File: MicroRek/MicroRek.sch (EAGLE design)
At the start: 41 parts, among them IC3 LSM9DS1TR

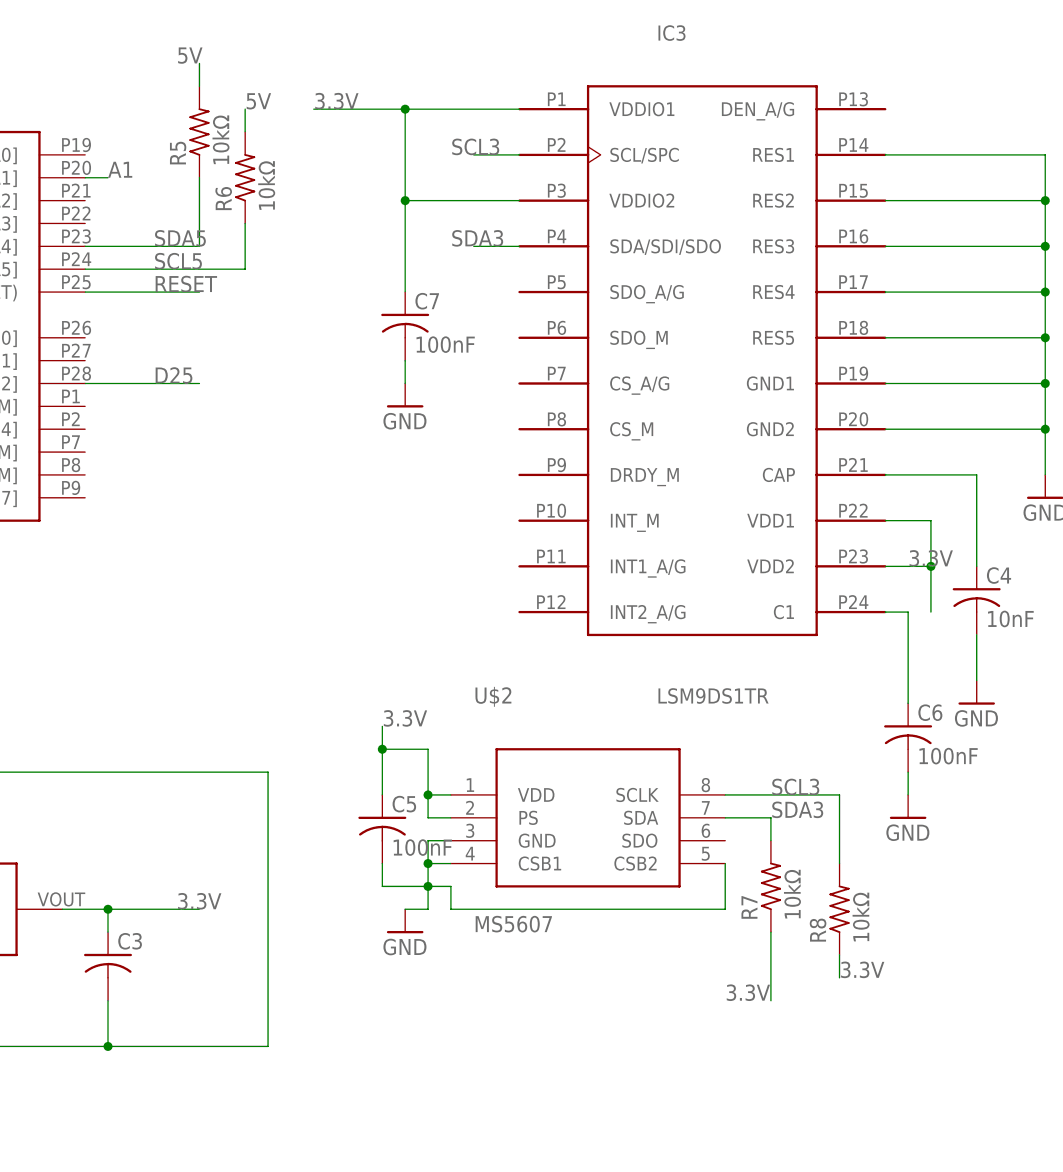
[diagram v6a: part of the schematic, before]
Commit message: fixed pullup resistors
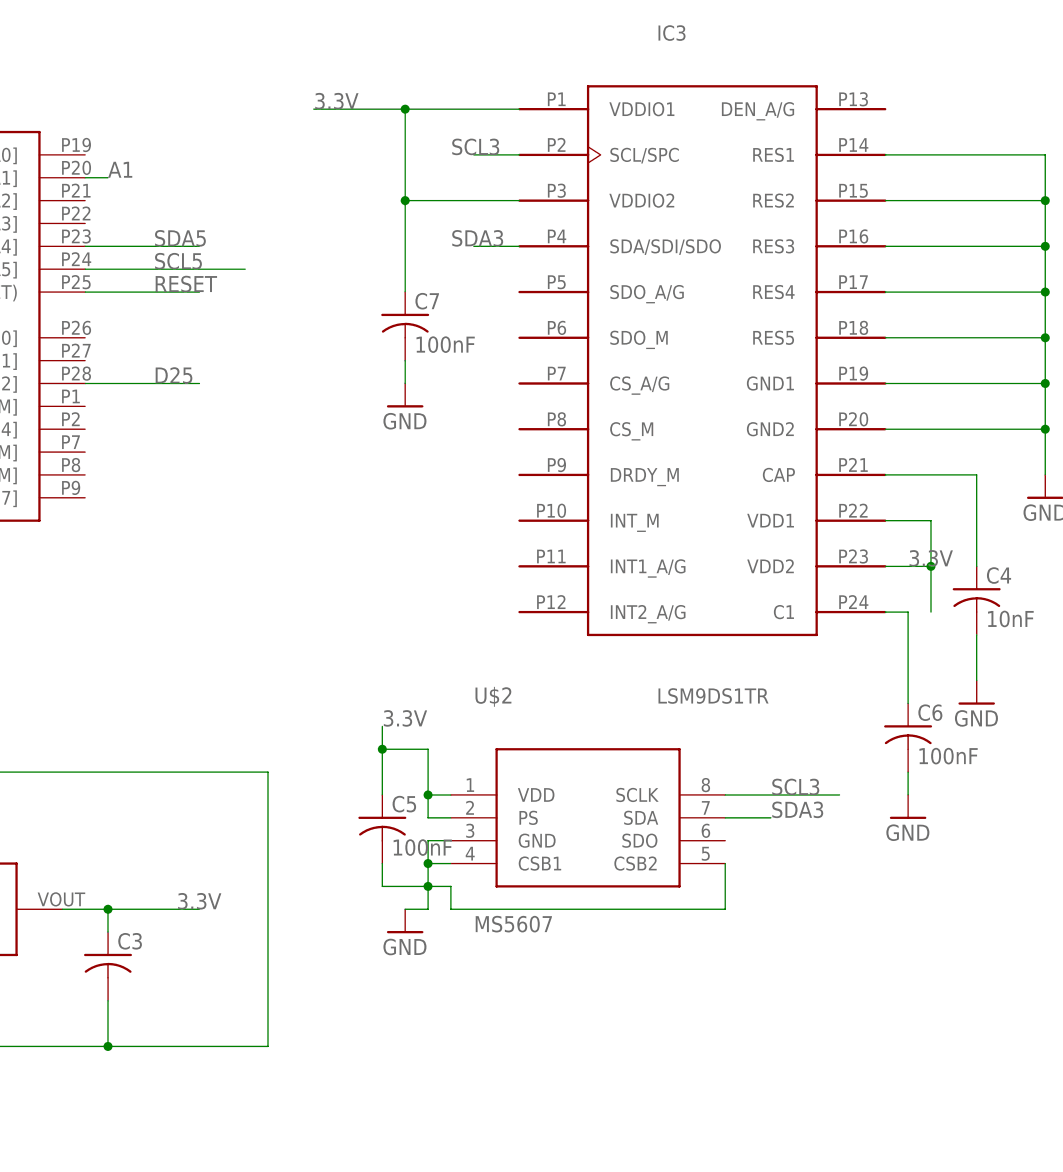
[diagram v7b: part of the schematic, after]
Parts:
- removed R5, R6, R7, R8: 10kΩ, resistor:R-US_R0603
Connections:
- net 3.3V: no longer R7.1, R8.1
- net 5V: no longer R5.2, R6.2
- net SCL3: no longer R8.2
- net SCL5: no longer R6.1
- net SDA3: no longer R7.2
- net SDA5: no longer R5.1
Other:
- note removed: "0805 LED"
- note removed: "100ohm for R3 100kohm for R2 4.7kohm R1 For LEDS"
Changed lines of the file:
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@@
 <part name="L1" library="CPSS" deviceset="L-US" device="" value="4.7 uH"/>
 <part name="R4" library="resistor" library_urn="urn:adsk.eagle:library:348" deviceset="R-US_" device="R0603" package3d_urn="urn:adsk.eagle:package:26057/1" value="100KΩ"/>
-<part name="R5" library="resistor" library_urn="urn:adsk.eagle:library:348" deviceset="R-US_" device="R0603" package3d_urn="urn:adsk.eagle:package:26057/1" value="10kΩ"/>
-<part name="R6" library="resistor" library_urn="urn:adsk.eagle:library:348" deviceset="R-US_" device="R0603" package3d_urn="urn:adsk.eagle:package:26057/1" value="10kΩ"/>
-<part name="R7" library="resistor" library_urn="urn:adsk.eagle:library:348" deviceset="R-US_" device="R0603" package3d_urn="urn:adsk.eagle:package:26057/1" value="10kΩ"/>
-<part name="R8" library="resistor" library_urn="urn:adsk.eagle:library:348" deviceset="R-US_" device="R0603" package3d_urn="urn:adsk.eagle:package:26057/1" value="10kΩ"/>
 <part name="U$8" library="CPSS_CONNECTOR" deviceset="MINI_ICSP" device=""/>
 <part name="GND10" library="supply1" library_urn="urn:adsk.eagle:library:371" deviceset="GND" device=""/>
@@
 <plain>
 <frame x1="0" y1="0" x2="279.4" y2="215.9" columns="8" rows="5" layer="97"/>
-<text x="193.04" y="83.82" size="1.778" layer="101">100ohm for R3
-100kohm for R2
-4.7kohm R1
-For LEDS</text>
-<text x="193.04" y="78.74" size="1.778" layer="101">0805 LED</text>
 </plain>
 <instances>
@@
 <instance part="L1" gate="G$1" x="96.52" y="109.22" rot="R90"/>
 <instance part="R4" gate="G$1" x="162.56" y="68.58"/>
-<instance part="R5" gate="G$1" x="167.64" y="195.58" rot="R90"/>
-<instance part="R6" gate="G$1" x="172.72" y="190.5" rot="R90"/>
-<instance part="R7" gate="G$1" x="231.14" y="111.76" rot="R90"/>
-<instance part="R8" gate="G$1" x="238.76" y="109.22" rot="R90"/>
 <instance part="U$8" gate="G$1" x="121.92" y="137.16"/>
 <instance part="GND10" gate="1" x="139.7" y="129.54"/>
@@
 </segment>
 <segment>
-<pinref part="R5" gate="G$1" pin="2"/>
-<wire x1="167.64" y1="200.66" x2="167.64" y2="203.2" width="0.1524" layer="91"/>
-<label x="165.1" y="203.2" size="1.778" layer="95"/>
-</segment>
-<segment>
-<pinref part="R6" gate="G$1" pin="2"/>
-<wire x1="172.72" y1="195.58" x2="172.72" y2="198.12" width="0.1524" layer="91"/>
-<label x="172.72" y="198.12" size="1.778" layer="95"/>
-</segment>
-<segment>
 <pinref part="R14" gate="G$1" pin="2"/>
 <wire x1="78.74" y1="68.58" x2="81.28" y2="68.58" width="0.1524" layer="91"/>
@@
 <wire x1="154.94" y1="182.88" x2="167.64" y2="182.88" width="0.1524" layer="91"/>
 <label x="162.56" y="182.88" size="1.778" layer="95"/>
-<wire x1="167.64" y1="182.88" x2="167.64" y2="190.5" width="0.1524" layer="91"/>
-<pinref part="R5" gate="G$1" pin="1"/>
 </segment>
 </net>
@@
 <wire x1="154.94" y1="180.34" x2="172.72" y2="180.34" width="0.1524" layer="91"/>
 <label x="162.56" y="180.34" size="1.778" layer="95"/>
-<wire x1="172.72" y1="180.34" x2="172.72" y2="185.42" width="0.1524" layer="91"/>
-<pinref part="R6" gate="G$1" pin="1"/>
 </segment>
 </net>
@@
 <wire x1="226.06" y1="119.38" x2="231.14" y2="119.38" width="0.1524" layer="91"/>
 <label x="231.14" y="119.38" size="1.778" layer="95"/>
-<wire x1="231.14" y1="119.38" x2="231.14" y2="116.84" width="0.1524" layer="91"/>
-<pinref part="R7" gate="G$1" pin="2"/>
 </segment>
 <segment>
@@
 <label x="231.14" y="121.92" size="1.778" layer="95"/>
 <wire x1="226.06" y1="121.92" x2="238.76" y2="121.92" width="0.1524" layer="91"/>
-<wire x1="238.76" y1="121.92" x2="238.76" y2="114.3" width="0.1524" layer="91"/>
-<pinref part="R8" gate="G$1" pin="2"/>
 </segment>
 <segment>
@@
 <label x="137.16" y="58.42" size="1.778" layer="95"/>
 </segment>
-<segment>
-<pinref part="R7" gate="G$1" pin="1"/>
-<wire x1="231.14" y1="106.68" x2="231.14" y2="99.06" width="0.1524" layer="91"/>
-<label x="226.06" y="99.06" size="1.778" layer="95"/>
-</segment>
-<segment>
-<pinref part="R8" gate="G$1" pin="1"/>
-<wire x1="238.76" y1="104.14" x2="238.76" y2="101.6" width="0.1524" layer="91"/>
-<label x="238.76" y="101.6" size="1.778" layer="95"/>
-</segment>
 </net>
 <net name="CPB6" class="0">
@@
 </drawing>
 <compatibility>
-<note version="6.3" minversion="6.2.2" severity="warning">
-Since Version 6.2.2 text objects can contain more than one line,
-which will not be processed correctly with this version.
-</note>
 <note version="8.2" severity="warning">
 Since Version 8.2, EAGLE supports online libraries. The ids

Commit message: Approved Final Schematic
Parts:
- removed R10, R11, R12, R17, R18, R19: 4.7kΩ, resistor:R-US_R0603
- R4: value 100KΩ -> 100Ω
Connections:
- net 3.3V: no longer R17.1, R18.1, R19.1
- net 5V: no longer R10.2, R11.2, R12.2
- net MISO3: no longer R19.2
- net MISO5: no longer R12.1
- net MOSI3: no longer R18.2
- net MOSI5: no longer R11.1
- net SCK3: no longer R17.2
- net SCK5: no longer R10.1
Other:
- moved on the sheet: R21
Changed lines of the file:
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@@
 <?xml version="1.0" encoding="utf-8"?>
 <!DOCTYPE eagle SYSTEM "eagle.dtd">
-<eagle version="9.0.0">
+<eagle version="8.7.1">
 <drawing>
 <settings>
-<setting alwaysvectorfont="no"/>
+<setting alwaysvectorfont="yes"/>
 <setting verticaltext="up"/>
 </settings>
@@
 <part name="LED2" library="led" library_urn="urn:adsk.eagle:library:259" deviceset="LED" device="CHIPLED_0805" package3d_urn="urn:adsk.eagle:package:15821/2"/>
 <part name="L1" library="CPSS" deviceset="L-US" device="" value="4.7 uH"/>
-<part name="R4" library="resistor" library_urn="urn:adsk.eagle:library:348" deviceset="R-US_" device="R0603" package3d_urn="urn:adsk.eagle:package:26057/1" value="100KΩ"/>
+<part name="R4" library="resistor" library_urn="urn:adsk.eagle:library:348" deviceset="R-US_" device="R0603" package3d_urn="urn:adsk.eagle:package:26057/1" value="100Ω"/>
 <part name="U$8" library="CPSS_CONNECTOR" deviceset="MINI_ICSP" device=""/>
 <part name="GND10" library="supply1" library_urn="urn:adsk.eagle:library:371" deviceset="GND" device=""/>
 <part name="R9" library="resistor" library_urn="urn:adsk.eagle:library:348" deviceset="R-US_" device="R0603" package3d_urn="urn:adsk.eagle:package:26057/1" value="4.7kΩ"/>
-<part name="R10" library="resistor" library_urn="urn:adsk.eagle:library:348" deviceset="R-US_" device="R0603" package3d_urn="urn:adsk.eagle:package:26057/1" value="4.7kΩ"/>
-<part name="R11" library="resistor" library_urn="urn:adsk.eagle:library:348" deviceset="R-US_" device="R0603" package3d_urn="urn:adsk.eagle:package:26057/1" value="4.7kΩ"/>
-<part name="R12" library="resistor" library_urn="urn:adsk.eagle:library:348" deviceset="R-US_" device="R0603" package3d_urn="urn:adsk.eagle:package:26057/1" value="4.7kΩ"/>
 <part name="R13" library="resistor" library_urn="urn:adsk.eagle:library:348" deviceset="R-US_" device="R0603" package3d_urn="urn:adsk.eagle:package:26057/1" value="4.7kΩ"/>
 <part name="R14" library="resistor" library_urn="urn:adsk.eagle:library:348" deviceset="R-US_" device="R0603" package3d_urn="urn:adsk.eagle:package:26057/1" value="4.7kΩ"/>
 <part name="R15" library="resistor" library_urn="urn:adsk.eagle:library:348" deviceset="R-US_" device="R0603" package3d_urn="urn:adsk.eagle:package:26057/1" value="4.7kΩ"/>
 <part name="R16" library="resistor" library_urn="urn:adsk.eagle:library:348" deviceset="R-US_" device="R0603" package3d_urn="urn:adsk.eagle:package:26057/1" value="4.7kΩ"/>
-<part name="R17" library="resistor" library_urn="urn:adsk.eagle:library:348" deviceset="R-US_" device="R0603" package3d_urn="urn:adsk.eagle:package:26057/1" value="4.7kΩ"/>
-<part name="R18" library="resistor" library_urn="urn:adsk.eagle:library:348" deviceset="R-US_" device="R0603" package3d_urn="urn:adsk.eagle:package:26057/1" value="4.7kΩ"/>
-<part name="R19" library="resistor" library_urn="urn:adsk.eagle:library:348" deviceset="R-US_" device="R0603" package3d_urn="urn:adsk.eagle:package:26057/1" value="4.7kΩ"/>
 <part name="R20" library="resistor" library_urn="urn:adsk.eagle:library:348" deviceset="R-US_" device="R0603" package3d_urn="urn:adsk.eagle:package:26057/1" value="4.7kΩ"/>
 <part name="GND2" library="supply1" library_urn="urn:adsk.eagle:library:371" deviceset="GND" device=""/>
@@
 <instance part="GND10" gate="1" x="139.7" y="129.54"/>
 <instance part="R9" gate="G$1" x="73.66" y="43.18"/>
-<instance part="R10" gate="G$1" x="73.66" y="48.26"/>
-<instance part="R11" gate="G$1" x="73.66" y="53.34"/>
-<instance part="R12" gate="G$1" x="73.66" y="58.42"/>
 <instance part="R13" gate="G$1" x="73.66" y="63.5"/>
 <instance part="R14" gate="G$1" x="73.66" y="68.58"/>
 <instance part="R15" gate="G$1" x="22.86" y="68.58"/>
 <instance part="R16" gate="G$1" x="22.86" y="43.18"/>
-<instance part="R17" gate="G$1" x="22.86" y="48.26"/>
-<instance part="R18" gate="G$1" x="22.86" y="53.34"/>
-<instance part="R19" gate="G$1" x="22.86" y="58.42"/>
 <instance part="R20" gate="G$1" x="22.86" y="63.5"/>
 <instance part="GND2" gate="1" x="210.82" y="33.02"/>
 <instance part="U$9" gate="G$2" x="195.58" y="66.04" rot="R90"/>
 <instance part="R2" gate="G$1" x="162.56" y="58.42"/>
-<instance part="R21" gate="G$1" x="195.58" y="33.02" rot="R90"/>
+<instance part="R21" gate="G$1" x="195.58" y="50.8" rot="R90"/>
 </instances>
 <busses>
@@
 </segment>
 <segment>
-<pinref part="R12" gate="G$1" pin="2"/>
-<wire x1="78.74" y1="58.42" x2="81.28" y2="58.42" width="0.1524" layer="91"/>
-<label x="81.28" y="58.42" size="1.778" layer="95"/>
-</segment>
-<segment>
-<pinref part="R11" gate="G$1" pin="2"/>
-<wire x1="78.74" y1="53.34" x2="81.28" y2="53.34" width="0.1524" layer="91"/>
-<label x="81.28" y="53.34" size="1.778" layer="95"/>
-</segment>
-<segment>
-<pinref part="R10" gate="G$1" pin="2"/>
-<wire x1="78.74" y1="48.26" x2="81.28" y2="48.26" width="0.1524" layer="91"/>
-<label x="81.28" y="48.26" size="1.778" layer="95"/>
-</segment>
-<segment>
 <pinref part="R9" gate="G$1" pin="2"/>
 <wire x1="78.74" y1="43.18" x2="81.28" y2="43.18" width="0.1524" layer="91"/>
@@
 <wire x1="63.5" y1="58.42" x2="68.58" y2="58.42" width="0.1524" layer="91"/>
 <label x="68.58" y="58.42" size="1.778" layer="95"/>
-<pinref part="R12" gate="G$1" pin="1"/>
 </segment>
 <segment>
@@
 <wire x1="63.5" y1="53.34" x2="68.58" y2="53.34" width="0.1524" layer="91"/>
 <label x="68.58" y="53.34" size="1.778" layer="95"/>
-<pinref part="R11" gate="G$1" pin="1"/>
 </segment>
 <segment>
@@
 <wire x1="63.5" y1="48.26" x2="68.58" y2="48.26" width="0.1524" layer="91"/>
 <label x="68.58" y="48.26" size="1.778" layer="95"/>
-<pinref part="R10" gate="G$1" pin="1"/>
 </segment>
 <segment>
@@
 <wire x1="33.02" y1="58.42" x2="27.94" y2="58.42" width="0.1524" layer="91"/>
 <label x="25.4" y="58.42" size="1.778" layer="95"/>
-<pinref part="R19" gate="G$1" pin="2"/>
 </segment>
 <segment>
@@
 <wire x1="33.02" y1="53.34" x2="27.94" y2="53.34" width="0.1524" layer="91"/>
 <label x="25.4" y="53.34" size="1.778" layer="95"/>
-<pinref part="R18" gate="G$1" pin="2"/>
 </segment>
 <segment>
@@
 <wire x1="33.02" y1="48.26" x2="27.94" y2="48.26" width="0.1524" layer="91"/>
 <label x="25.4" y="48.26" size="1.778" layer="95"/>
-<pinref part="R17" gate="G$1" pin="2"/>
 </segment>
 <segment>
@@
 </segment>
 <segment>
-<pinref part="R19" gate="G$1" pin="1"/>
-<wire x1="17.78" y1="58.42" x2="15.24" y2="58.42" width="0.1524" layer="91"/>
-<label x="12.7" y="58.42" size="1.778" layer="95"/>
-</segment>
-<segment>
-<pinref part="R18" gate="G$1" pin="1"/>
-<wire x1="17.78" y1="53.34" x2="15.24" y2="53.34" width="0.1524" layer="91"/>
-<label x="12.7" y="53.34" size="1.778" layer="95"/>
-</segment>
-<segment>
-<pinref part="R17" gate="G$1" pin="1"/>
-<wire x1="17.78" y1="48.26" x2="15.24" y2="48.26" width="0.1524" layer="91"/>
-<label x="12.7" y="48.26" size="1.778" layer="95"/>
-</segment>
-<segment>
 <pinref part="R16" gate="G$1" pin="1"/>
 <wire x1="17.78" y1="43.18" x2="15.24" y2="43.18" width="0.1524" layer="91"/>
@@
 <segment>
 <pinref part="R21" gate="G$1" pin="1"/>
-<wire x1="195.58" y1="27.94" x2="195.58" y2="22.86" width="0.1524" layer="91"/>
-<wire x1="195.58" y1="22.86" x2="182.88" y2="22.86" width="0.1524" layer="91"/>
-<label x="182.88" y="22.86" size="1.778" layer="95"/>
+<wire x1="195.58" y1="45.72" x2="195.58" y2="40.64" width="0.1524" layer="91"/>
+<wire x1="195.58" y1="40.64" x2="182.88" y2="40.64" width="0.1524" layer="91"/>
+<label x="182.88" y="40.64" size="1.778" layer="95"/>
 </segment>
 </net>
@@
 <pinref part="U$9" gate="G$2" pin="B"/>
 <pinref part="R21" gate="G$1" pin="2"/>
-<wire x1="195.58" y1="63.5" x2="195.58" y2="38.1" width="0.1524" layer="91"/>
-</segment>
-</net>
+<wire x1="195.58" y1="63.5" x2="195.58" y2="55.88" width="0.1524" layer="91"/>
+</segment>
+</net>
